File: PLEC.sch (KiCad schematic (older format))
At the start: 5 parts, among them J1 Conn_01x02, J2 Conn_01x02, J3 Conn_01x03, J4 Conn_01x06, J5 Conn_01x04

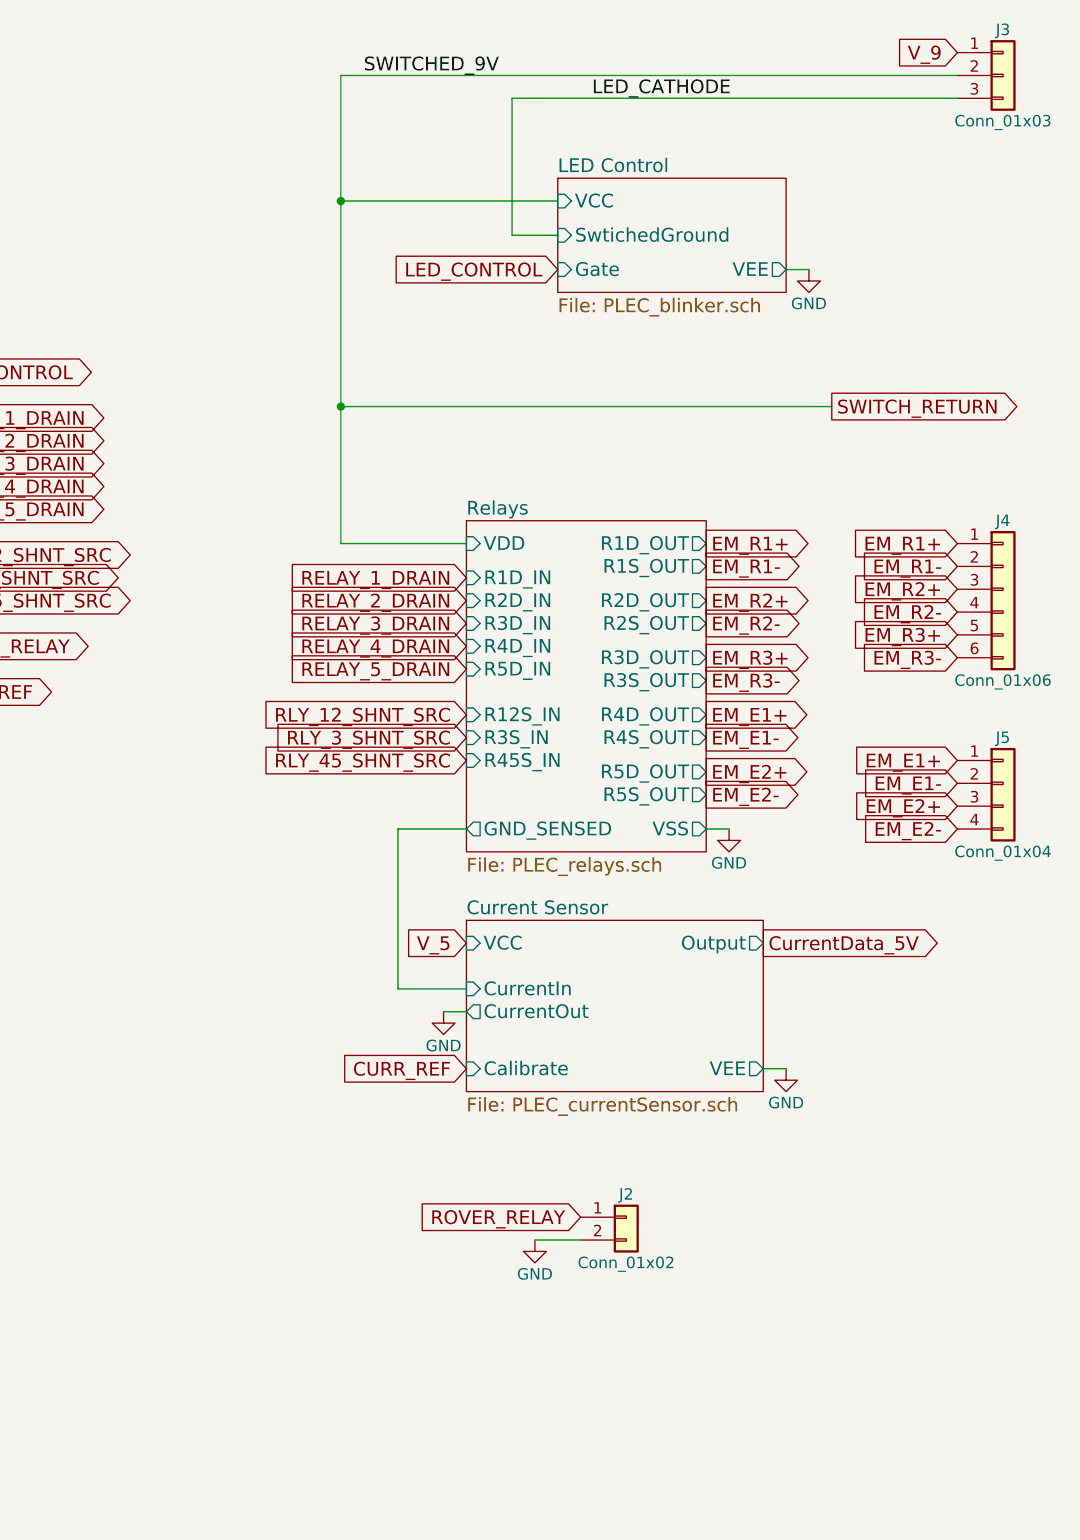
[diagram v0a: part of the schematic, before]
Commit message: Almost done with layout; need to rearrange uC pins
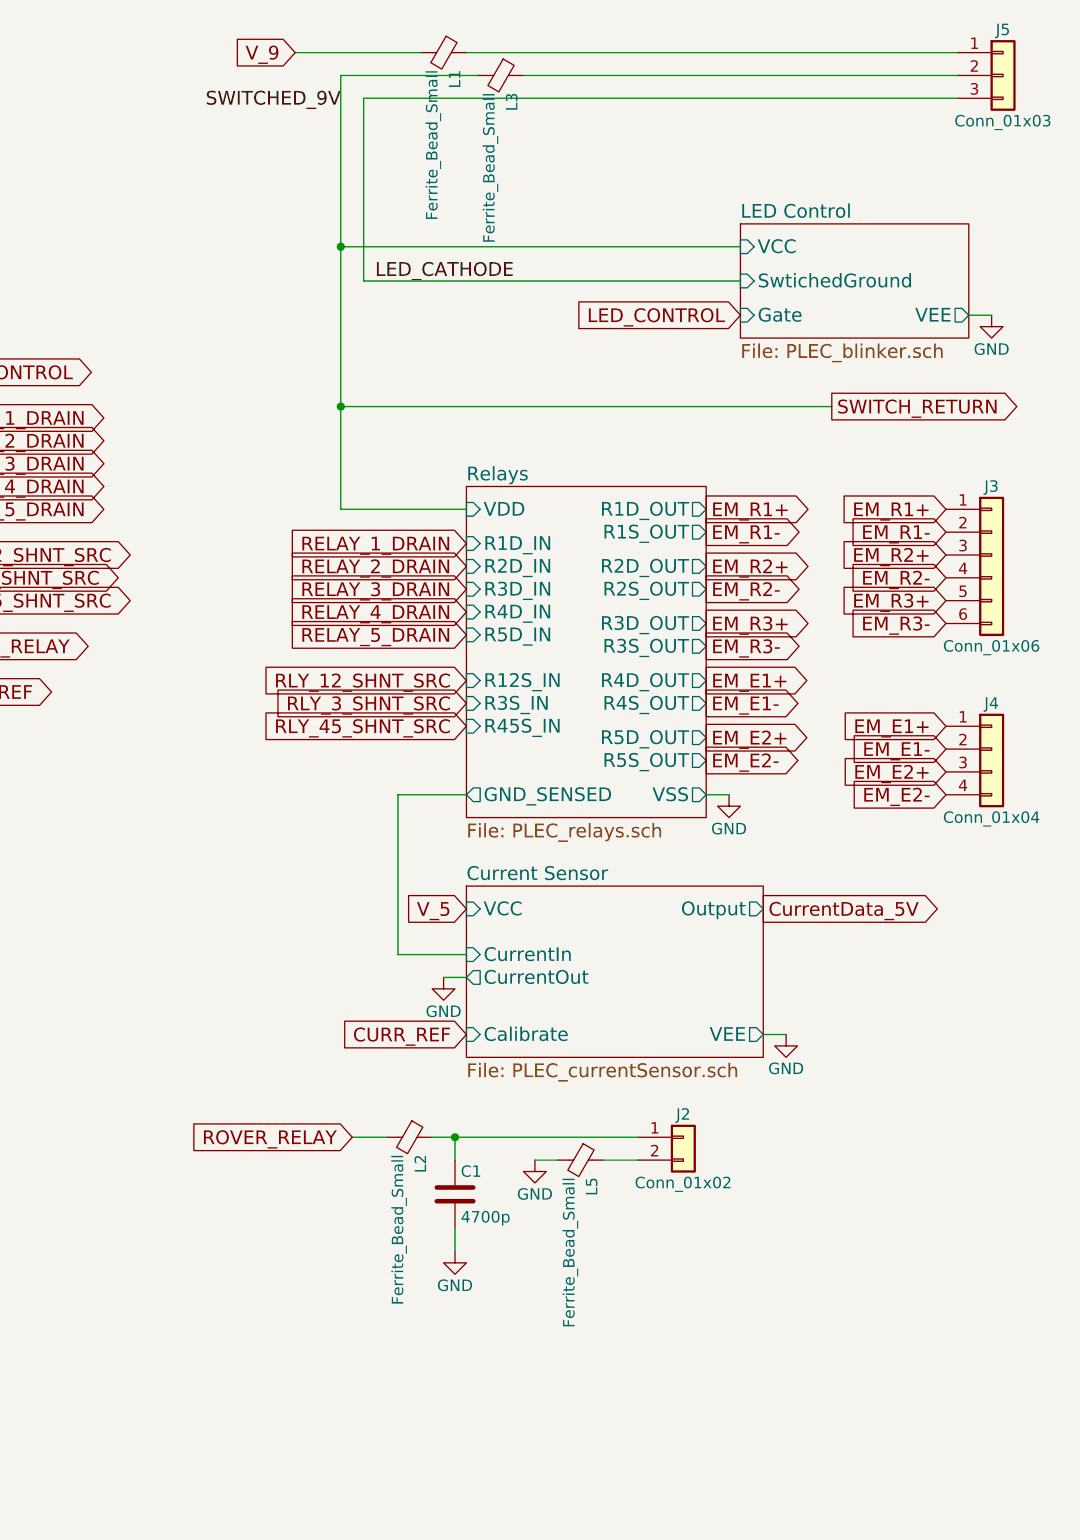
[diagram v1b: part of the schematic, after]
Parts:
- added C1: 4700p, PLEC:THTt_100Px150Lx100Wx183H_4700p, symbol C
- added L1, L2, L3, L5: Ferrite_Bead_Small, Inductors_THT:L_Axial_L7.0mm_D3.3mm_P5.08mm_Vertical_Fastron_MICC, symbol Ferrite_Bead_Small
- renumbered J4 to J3, J5 to J4, J3 to J5
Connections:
- net GND: now also C1.2, L5.2; no longer J2.2 (Pin_2)
- net ROVER_RELAY: now also L2.2; no longer J2.1 (Pin_1)
- net SWITCH_RETURN: now also L3.2; no longer J5.2 (Pin_2)
- net V_9: now also L1.2; no longer J5.1 (Pin_1)
- new net: J5.1 (Pin_1), L1.1
- new net: J5.2 (Pin_2), L3.1
- new net: C1.1, J2.1 (Pin_1), L2.1
- new net: J2.2 (Pin_2), L5.1
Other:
- moved on the sheet: J2, J3, J4

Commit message: Finished PCB with no errors
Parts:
- added C29: 4700p, PLEC:THTt_100Px150Lx100Wx183H_4700p, symbol C
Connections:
- net GND: no longer C1.2
- net V9_Out: now reaches J5.1 (Pin_1), L1.1
- net V9_Out: now also C29.2
- net SW_IN: now reaches J5.2 (Pin_2), L3.1
- net SW_IN: now also C29.1
- net at J2.2 (Pin_2), L5.1: now also C1.2
- net Power Rails/VCC_9 renamed V_Bat
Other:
- moved on the sheet: C1, J2, L5
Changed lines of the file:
@@
 L Conn_01x02 J2
 U 1 1 5A759C02
-P 9500 5550
-F 0 "J2" H 9500 5650 50  0000 C CNN
-F 1 "Conn_01x02" H 9500 5350 50  0000 C CNN
-F 2 "PLEC:THT_TerminalBlock_2.5mm_2pos" H 9500 5550 50  0001 C CNN
-F 3 "" H 9500 5550 50  0001 C CNN
-	1    9500 5550
+P 9750 5550
+F 0 "J2" H 9750 5650 50  0000 C CNN
+F 1 "Conn_01x02" H 9750 5350 50  0000 C CNN
+F 2 "PLEC:THT_TerminalBlock_2.5mm_2pos" H 9750 5550 50  0001 C CNN
+F 3 "" H 9750 5550 50  0001 C CNN
+	1    9750 5550
 	1    0    0    -1
 $EndComp
@@
 L GND #PWR07
 U 1 1 5A759FAD
-P 8850 5650
-F 0 "#PWR07" H 8850 5400 50  0001 C CNN
-F 1 "GND" H 8850 5500 50  0000 C CNN
-F 2 "" H 8850 5650 50  0001 C CNN
-F 3 "" H 8850 5650 50  0001 C CNN
-	1    8850 5650
+P 8550 6050
+F 0 "#PWR07" H 8550 5800 50  0001 C CNN
+F 1 "GND" H 8550 5900 50  0000 C CNN
+F 2 "" H 8550 6050 50  0001 C CNN
+F 3 "" H 8550 6050 50  0001 C CNN
+	1    8550 6050
 	-1   0    0    -1
 $EndComp
@@
 Wire Wire Line
 	8000 900  8000 2800
-Wire Wire Line
-	9750 1650 8000 1650
-Connection ~ 8000 1650
 Text Label 8000 1050 2    60   ~ 0
 SWITCHED_9V
@@
 	8800 900  10700 900
 Wire Wire Line
-	10700 800  8550 800
+	8550 800  10700 800
 Wire Wire Line
 	8100 1000 10700 1000
@@
 L C C1
 U 1 1 5A7CFDC2
-P 8500 5800
-F 0 "C1" H 8525 5900 50  0000 L CNN
-F 1 "4700p" H 8525 5700 50  0000 L CNN
-F 2 "PLEC:THTt_100Px150Lx100Wx183H_4700p" H 8538 5650 50  0001 C CNN
-F 3 "" H 8500 5800 50  0001 C CNN
-	1    8500 5800
-	1    0    0    -1
-$EndComp
-Connection ~ 8500 5550
-Wire Wire Line
-	8500 5950 8500 6050
-$Comp
-L GND #PWR010
-U 1 1 5A7D06C2
-P 8500 6050
-F 0 "#PWR010" H 8500 5800 50  0001 C CNN
-F 1 "GND" H 8500 5900 50  0000 C CNN
-F 2 "" H 8500 6050 50  0001 C CNN
-F 3 "" H 8500 6050 50  0001 C CNN
-	1    8500 6050
-	-1   0    0    -1
-$EndComp
+P 9000 5800
+F 0 "C1" H 9025 5900 50  0000 L CNN
+F 1 "4700p" H 9025 5700 50  0000 L CNN
+F 2 "PLEC:THTt_100Px150Lx100Wx183H_4700p" H 9038 5650 50  0001 C CNN
+F 3 "" H 9000 5800 50  0001 C CNN
+	1    9000 5800
+	1    0    0    -1
+$EndComp
+Connection ~ 9000 5550
 $Comp
 L Ferrite_Bead_Small L2
@@
 $EndComp
 Wire Wire Line
-	8400 5550 9300 5550
+	8400 5550 9550 5550
 $Comp
 L Ferrite_Bead_Small L5
 U 1 1 5A7DA73C
-P 9050 5650
-F 0 "L5" H 9125 5700 50  0000 L CNN
-F 1 "Ferrite_Bead_Small" H 9125 5600 50  0000 L CNN
-F 2 "Inductors_THT:L_Axial_L7.0mm_D3.3mm_P5.08mm_Vertical_Fastron_MICC" V 8980 5650 50  0001 C CNN
-F 3 "" H 9050 5650 50  0001 C CNN
-	1    9050 5650
+P 8800 6050
+F 0 "L5" H 8875 6100 50  0000 L CNN
+F 1 "Ferrite_Bead_Small" H 8875 6000 50  0000 L CNN
+F 2 "Inductors_THT:L_Axial_L7.0mm_D3.3mm_P5.08mm_Vertical_Fastron_MICC" V 8730 6050 50  0001 C CNN
+F 3 "" H 8800 6050 50  0001 C CNN
+	1    8800 6050
 	0    1    1    0
 $EndComp
 Wire Wire Line
-	8950 5650 8850 5650
-Wire Wire Line
-	9150 5650 9300 5650
+	8700 6050 8550 6050
 Wire Wire Line
 	8050 5550 8200 5550
 Wire Wire Line
-	8500 5650 8500 5550
+	9000 5650 9000 5550
+Text Label 1200 1100 0    60   ~ 0
+V_Bat
+Text Label 9550 800  0    60   ~ 0
+V9_Out
+Text Label 9550 900  0    60   ~ 0
+SW_IN
+Wire Wire Line
+	9750 1650 9300 1650
+Wire Wire Line
+	9300 1650 9300 900
+Connection ~ 9300 900
+Wire Wire Line
+	9550 5650 9400 5650
+Wire Wire Line
+	9400 5650 9400 6050
+Wire Wire Line
+	9400 6050 8900 6050
+Wire Wire Line
+	9000 5950 9000 6050
+Connection ~ 9000 6050
+$Comp
+L GND #PWR010
+U 1 1 5A7FC17E
+P 6300 5150
+F 0 "#PWR010" H 6300 4900 50  0001 C CNN
+F 1 "GND" H 6300 5000 50  0000 C CNN
+F 2 "" H 6300 5150 50  0001 C CNN
+F 3 "" H 6300 5150 50  0001 C CNN
+	1    6300 5150
+	1    0    0    -1
+$EndComp
+Wire Wire Line
+	6200 5150 6300 5150
+$Comp
+L C C29
+U 1 1 5A7FF5F3
+P 10550 1200
+F 0 "C29" H 10575 1300 50  0000 L CNN
+F 1 "4700p" H 10575 1100 50  0000 L CNN
+F 2 "PLEC:THTt_100Px150Lx100Wx183H_4700p" H 10588 1050 50  0001 C CNN
+F 3 "" H 10550 1200 50  0001 C CNN
+	1    10550 1200
+	-1   0    0    1
+$EndComp
+Wire Wire Line
+	10200 900  10200 1400
+Connection ~ 10200 900
+Wire Wire Line
+	10550 800  10550 1050
+Connection ~ 10550 800
+Wire Wire Line
+	10550 1350 10550 1400
+Wire Wire Line
+	10550 1400 10200 1400
 $EndSCHEMATC

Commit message: Added logo and schematic PDF
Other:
- note added: "Payload Ejection Controller Top View"

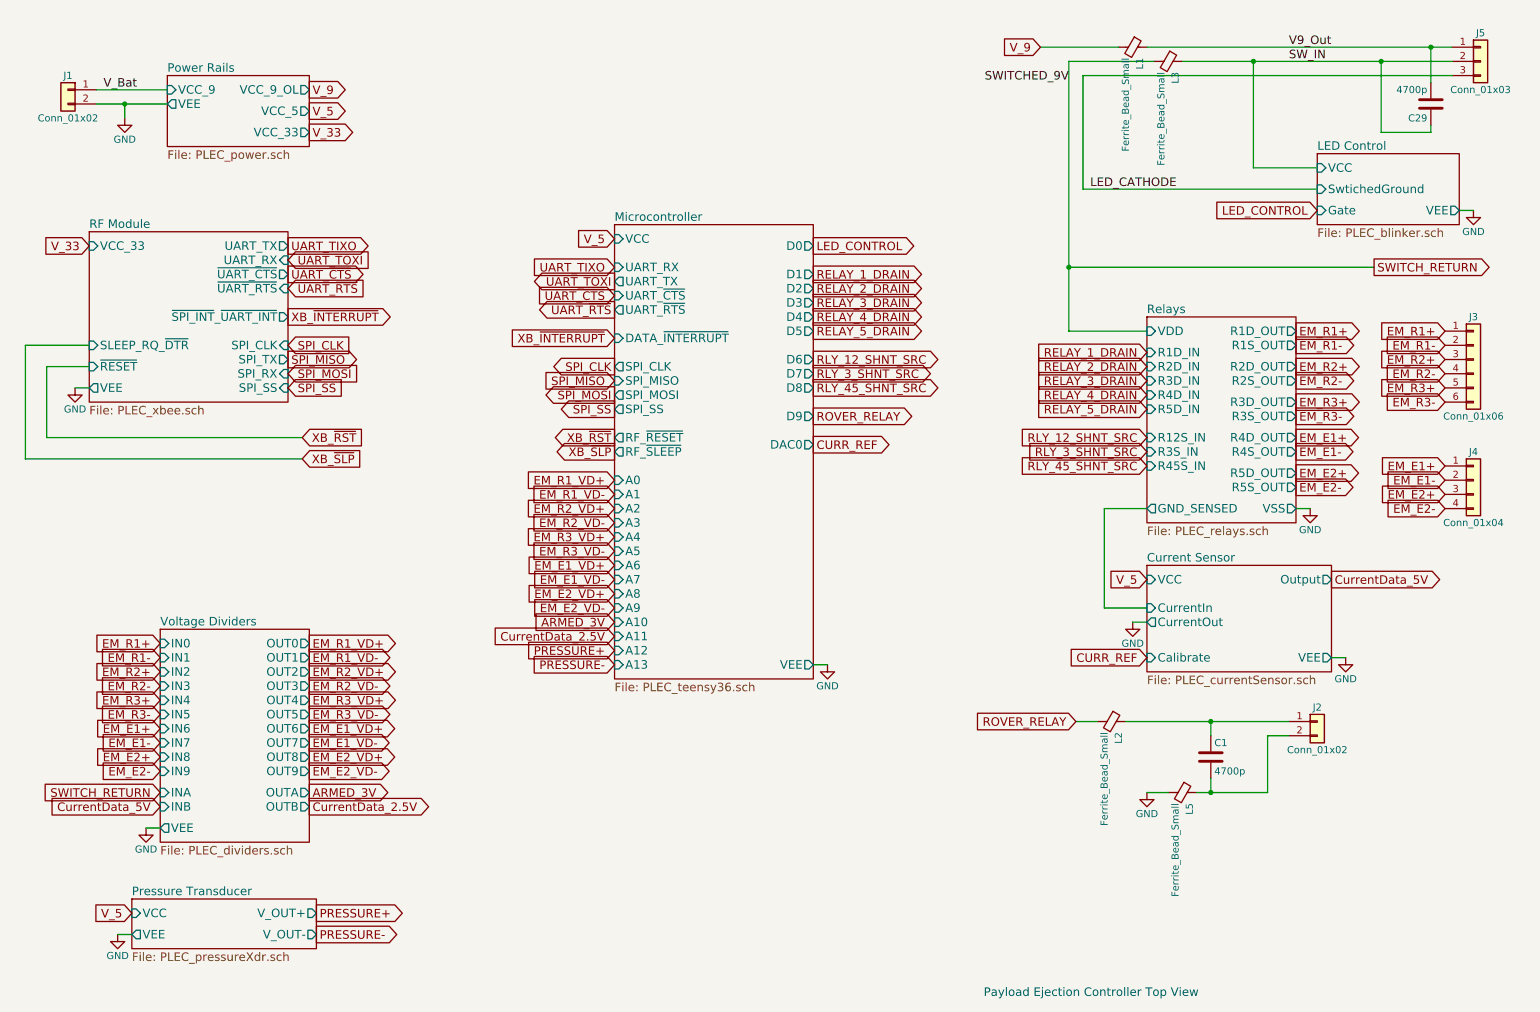
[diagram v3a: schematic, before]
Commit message: Replaced solid state relays with NPN Darlingtons
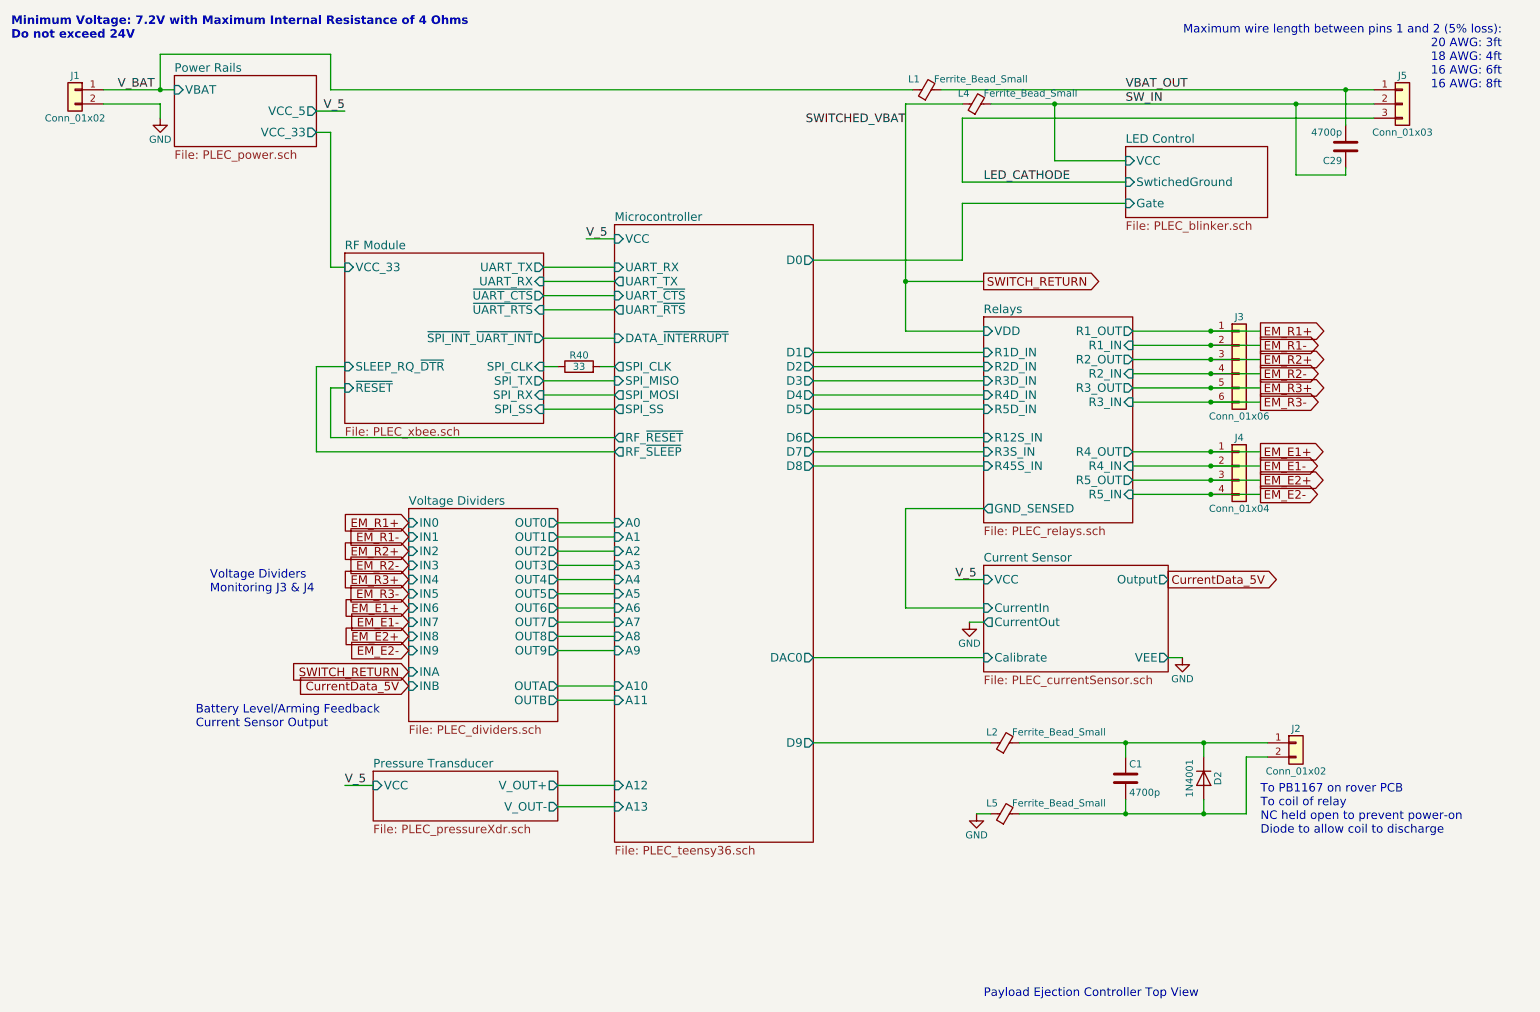
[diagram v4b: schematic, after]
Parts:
- removed L3: Ferrite_Bead_Small, Inductors_THT:L_Axial_L7.0mm_D3.3mm_P5.08mm_Vertical_Fastron_MICC, symbol Ferrite_Bead_Small
- added D2: 1N4001, Diodes_THT:D_DO-41_SOD81_P2.54mm_Vertical_KathodeUp, symbol D
- added L4: Ferrite_Bead_Small, Inductors_THT:L_Axial_L7.0mm_D3.3mm_P5.08mm_Vertical_Fastron_MICC, symbol Ferrite_Bead_Small
- added R40: 33, Resistors_THT:R_Axial_DIN0204_L3.6mm_D1.6mm_P5.08mm_Horizontal, symbol R
- J1: footprint PLEC:THT_TerminalBlock_2.5mm_2pos -> Connectors_Terminal_Blocks:TerminalBlock_Altech_AK300-2_P5.00mm
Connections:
- net ROVER_RELAY is gone; now on an unnamed net: L2.2
- net V_9 is gone; now on net VBAT_OUT: L1.2
- net GND: now also L5.1; no longer L5.2
- net SWITCH_RETURN: now also L4.1
- net SW_IN: now also L4.2
- net at C1.1, J2.1 (Pin_1): now also D2.1 (K); no longer L2.1
- net at C1.2, J2.2 (Pin_2): now also L5.2, D2.2 (A); no longer L5.1
- net V9_Out renamed VBAT_OUT
- net VBAT_OUT: no longer L1.1
- net V_Bat renamed V_BAT
- net V_BAT: now also L1.1
- new net Microcontroller/D9: L2.1
- new net Microcontroller/SPI_CLK: R40.2
- new net RF Module/SPI_CLK: R40.1
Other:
- note added: "Battery Level/Arming Feedback\nCurrent Sensor Output"
- note added: "Maximum wire length between pins 1 and 2 (5% loss):\n20 AWG: 3ft\n18 AWG: 4ft\n16 AWG: 6ft\n16 AWG: 8ft\n"
- note added: "Minimum Voltage: 7.2V with Maximum Internal Resistance of 4 Ohms\nDo not exceed 24V"
- note added: "To PB1167 on rover PCB\nTo coil of relay\nNC held open to prevent power-on\nDiode to allow coil to discharge"
- note added: "Voltage Dividers\nMonitoring J3 & J4\n"
- moved on the sheet: C1, C29, J1, J2, J3, J4, J5, L1
